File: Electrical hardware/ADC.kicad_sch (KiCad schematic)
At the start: 1 part, among them U2 LTC2299xUP

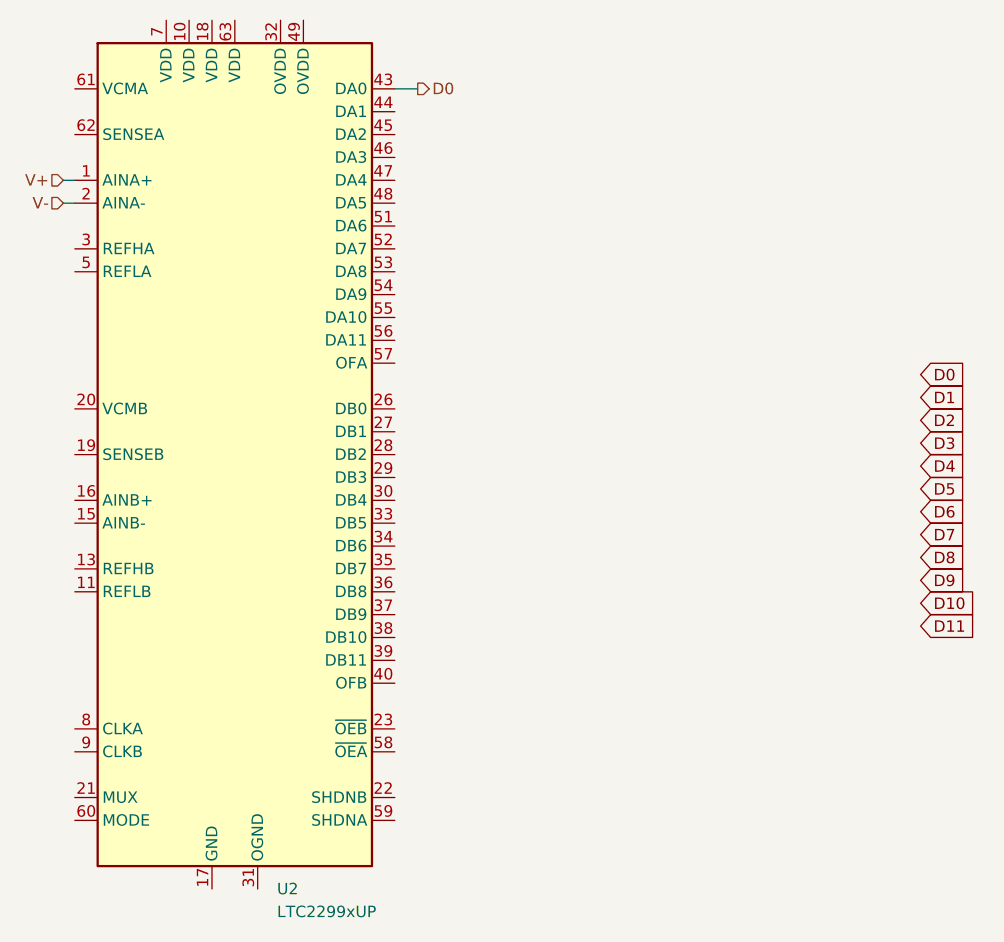
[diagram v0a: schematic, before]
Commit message: Created ADC footprint and extracted most important data from the data sheet
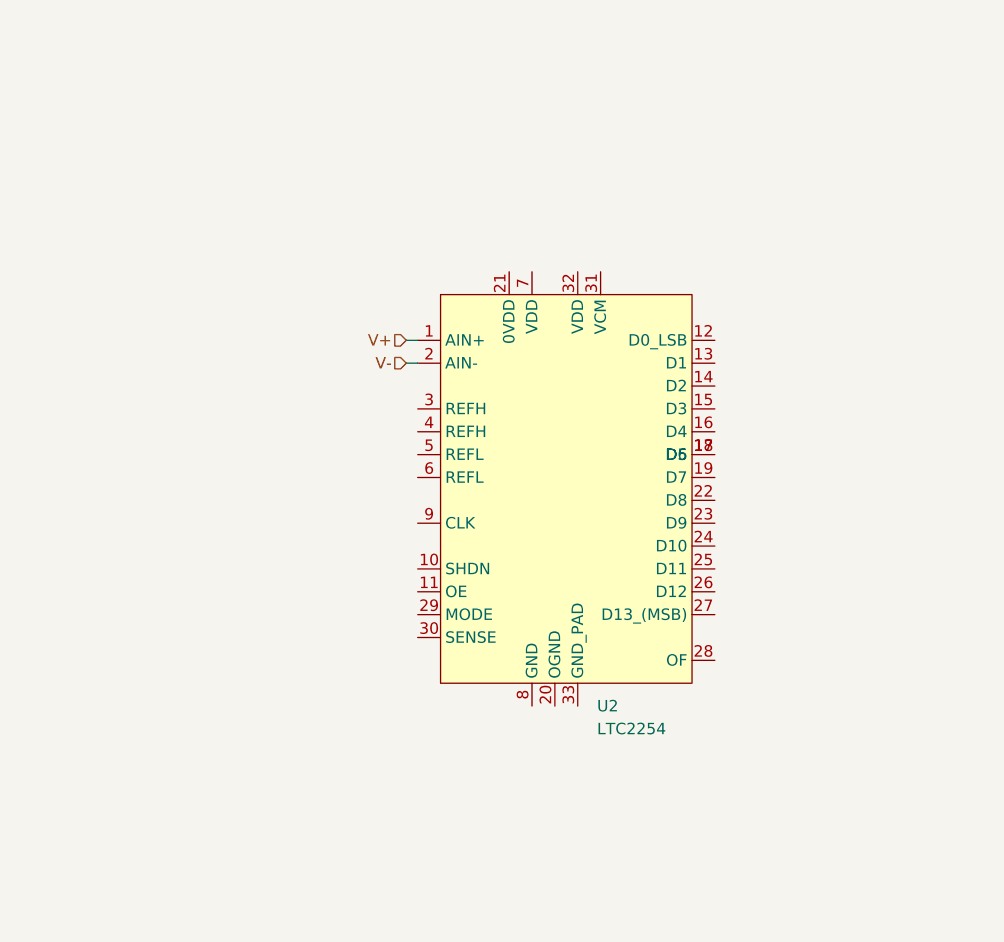
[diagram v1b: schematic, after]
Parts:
- removed U2: LTC2299xUP, Package_DFN_QFN:QFN-64-1EP_9x9mm_P0.5mm_EP7.15x7.15mm, symbol Analog_ADC:LTC2299xUP
- added U2: LTC2254, Package_DFN_QFN:QFN-32-1EP_5x5mm_P0.5mm_EP3.45x3.45mm, symbol LCMScopeLib:LTC2254
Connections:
- net V+: now also U2.1 (AIN+)
- net V-: now also U2.2 (AIN-)
- new net: U2.17 (D5), U2.18 (D6)
